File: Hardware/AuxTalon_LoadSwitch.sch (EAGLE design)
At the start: 89 parts, among them J1 CONN_AUX_M12_REMOTE, J2 CONN_AUX_M12_REMOTE, J3 CONN_AUX_M12_REMOTE, J4 CONN_TALON_REMOTE, U1 ADS1115, U11 MCP23018QFN, U16 MAX9064, U17 MAX9064, U18 SN74AUP1T87, U19 MAX9064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

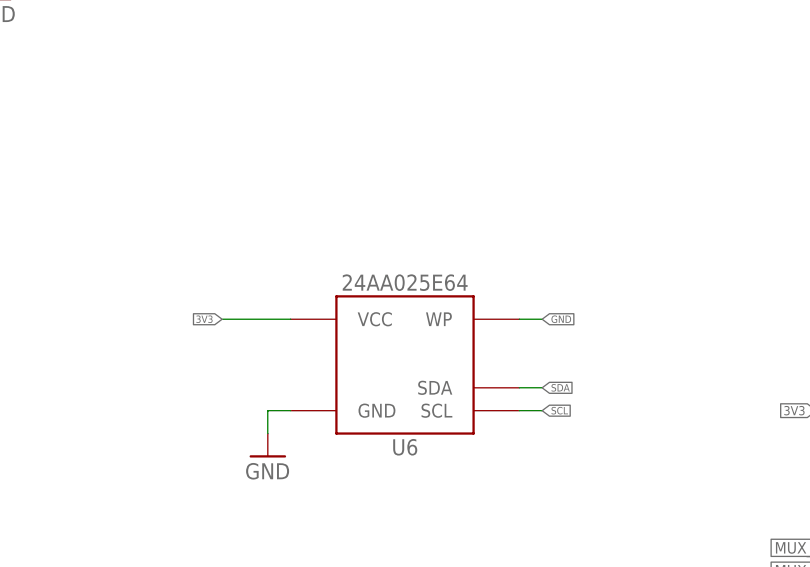
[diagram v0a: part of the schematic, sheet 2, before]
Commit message: Updates for modified BoM
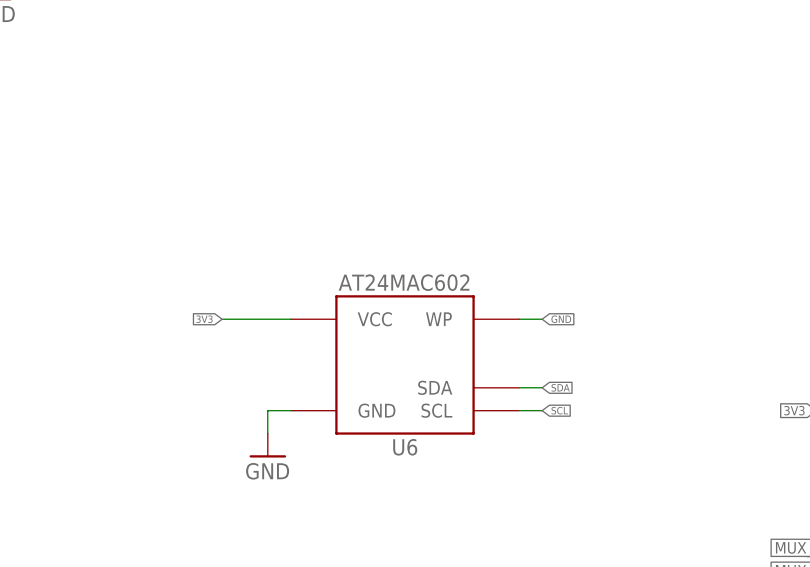
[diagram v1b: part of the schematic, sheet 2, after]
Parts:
- R10: device bschulz_passives:R-EU_100KR0402 -> bschulz_passives:R-EU_100KR0603
- U6: value 24AA02SOT23 -> AT24MAC602SOT23; device bschulz:24AA02SOT23 -> bschulz:AT24MAC602SOT23
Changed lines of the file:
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@@
 <part name="GND22" library="supply1" library_urn="urn:adsk.eagle:library:371" deviceset="GND" device=""/>
 <part name="GND23" library="supply1" library_urn="urn:adsk.eagle:library:371" deviceset="GND" device=""/>
-<part name="U6" library="bschulz" deviceset="24AA02" device="SOT23"/>
+<part name="U6" library="bschulz" deviceset="AT24MAC*02" device="SOT23" technology="6" value="AT24MAC602SOT23"/>
 <part name="GND24" library="supply1" library_urn="urn:adsk.eagle:library:371" deviceset="GND" device=""/>
 <part name="U7" library="bschulz" deviceset="74HC4852" device=""/>
@@
 <part name="C8" library="bschulz_passives" deviceset="C-EU" device="C0805" technology="10UF" value="10uF"/>
 <part name="GND51" library="supply1" library_urn="urn:adsk.eagle:library:371" deviceset="GND" device=""/>
-<part name="R10" library="bschulz_passives" deviceset="R-EU_" device="R0402" technology="100K" value="100k"/>
+<part name="R10" library="bschulz_passives" deviceset="R-EU_" device="R0603" technology="100K" value="100k"/>
 <part name="GND52" library="supply1" library_urn="urn:adsk.eagle:library:371" deviceset="GND" device=""/>
 <part name="GND53" library="supply1" library_urn="urn:adsk.eagle:library:371" deviceset="GND" device=""/>

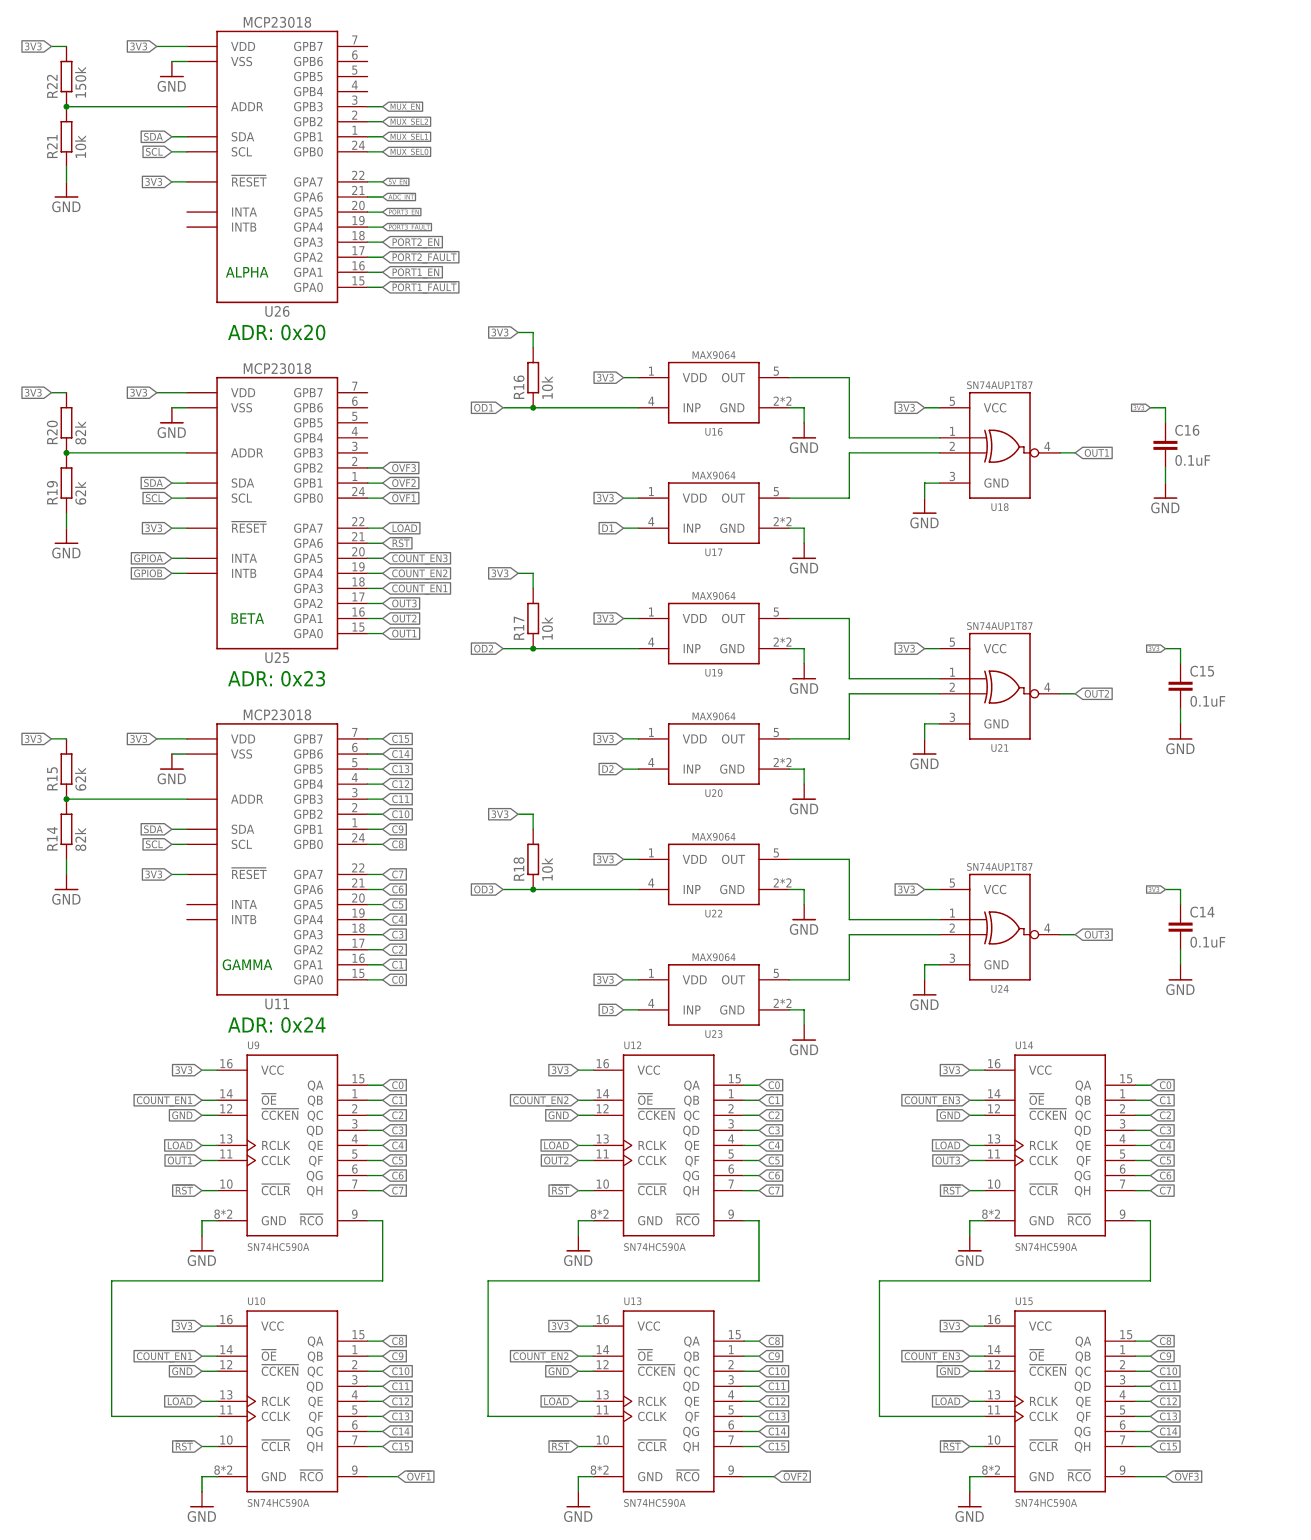
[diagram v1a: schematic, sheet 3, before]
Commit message: v1.4 Updates
Updated schematic and layout, boards sent to fab
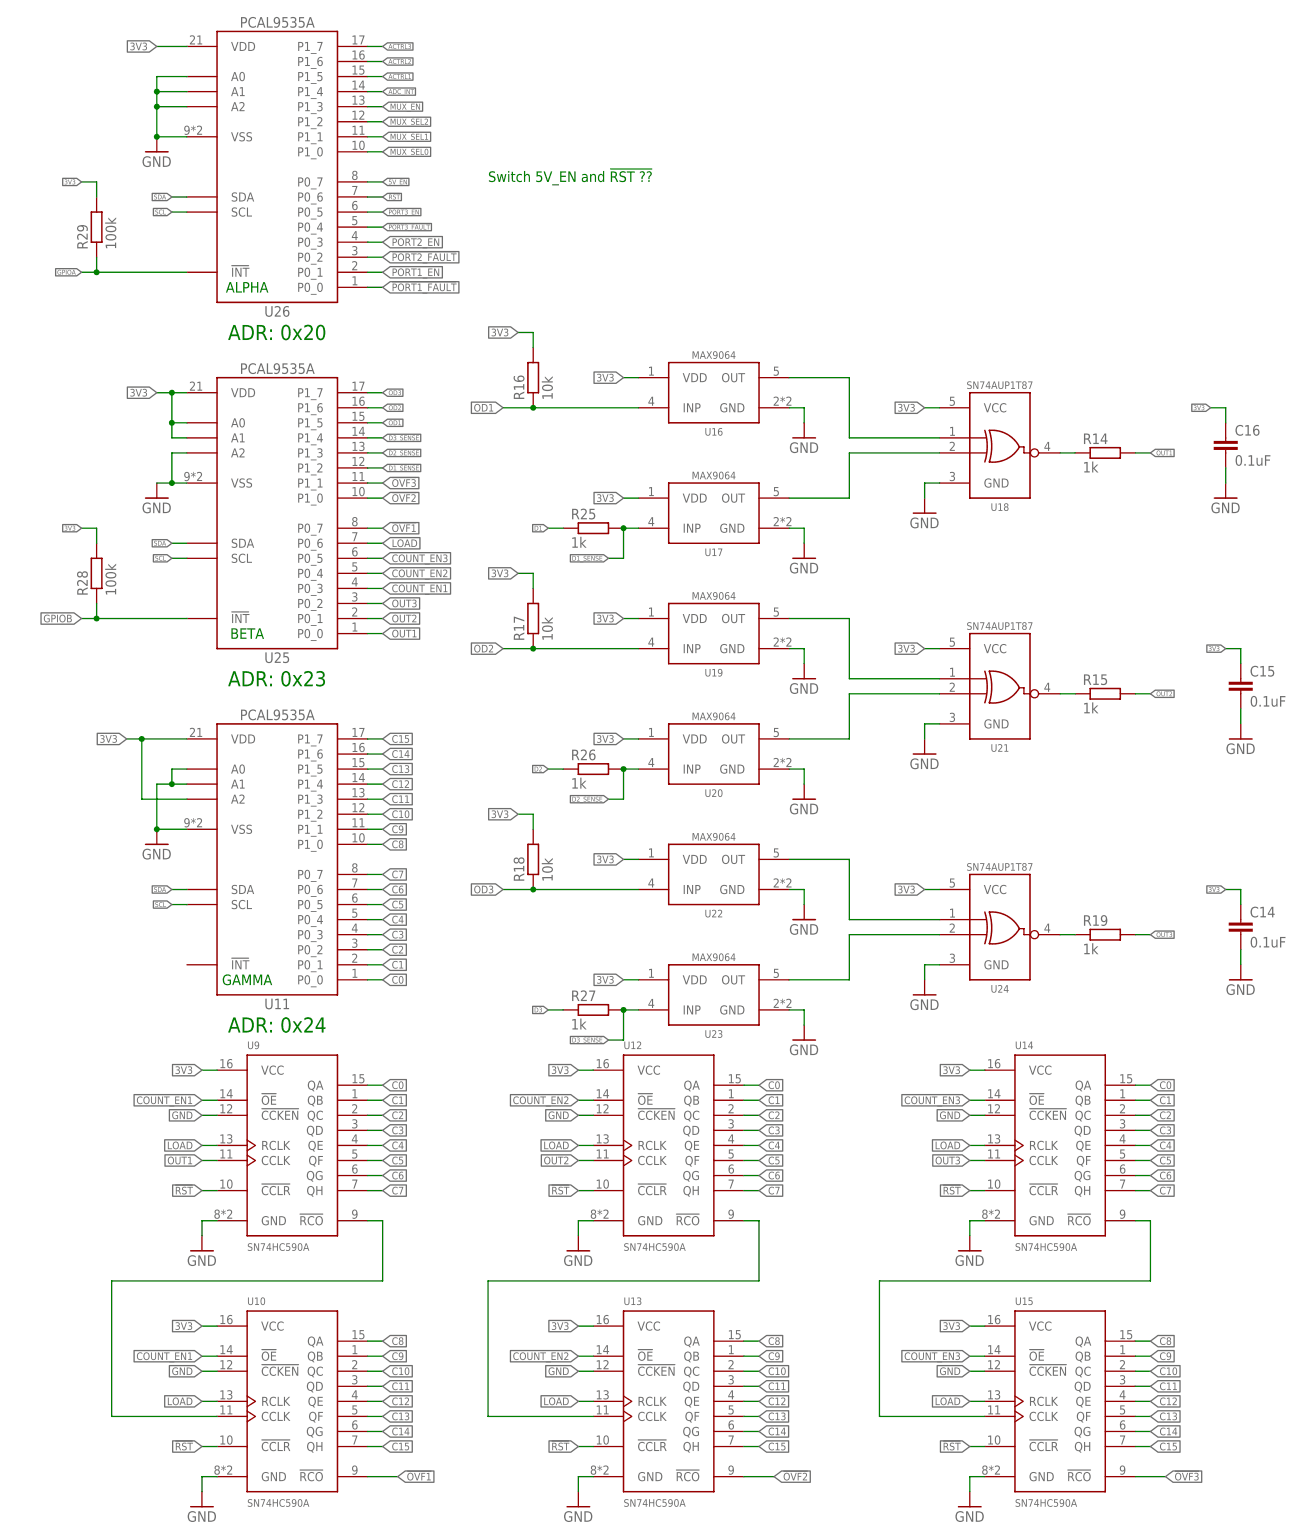
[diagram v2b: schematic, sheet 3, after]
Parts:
- added Q1, Q2, Q3: 2N7002, bschulz:MOSFET-NCH-2N7002P
- added R25, R26, R27: 1k, bschulz_passives:R-EU_1KR0402
- added R28, R29: 100k, bschulz_passives:R-EU_100KR0402
- R14: value 82k -> 1k; device bschulz_passives:R-EU_82KR0603 -> bschulz_passives:R-EU_1KR0402
- R15, R19: value 62k -> 1k; device bschulz_passives:R-EU_62KR0603 -> bschulz_passives:R-EU_1KR0402
- R20: value 82k -> 10k; device bschulz_passives:R-EU_82KR0603 -> bschulz_passives:R-EU_10KR0402
- R21: device bschulz_passives:R-EU_10KR0603 -> bschulz_passives:R-EU_10KR0402
- R22: value 150k -> 10k; device bschulz_passives:R-EU_150KR0603 -> bschulz_passives:R-EU_10KR0402
- U11, U25, U26: value MCP23018QFN -> PCAL9535AQFN; device bschulz:MCP23018QFN -> bschulz:PCAL9535AQFN
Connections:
- new net ACTRL1: Q1.G, U26.P1_5
- new net ACTRL2: Q2.G, U26.P1_6
- new net ACTRL3: Q3.G, U26.P1_7
- new net D1_SENSE: R25.2, U17.INP, U25.P1_2
- new net D2_SENSE: R26.2, U20.INP, U25.P1_3
- new net D3_SENSE: R27.2, U23.INP, U25.P1_4
- new net N$15: Q1.D, R20.1
- new net N$17: R15.1, U21.Y
- new net N$19: R19.1, U24.Y
- net !OVF1: now also U25.P0_7; no longer U25.GPB0
- net !OVF2: now also U25.P1_0; no longer U25.GPB1
- net !OVF3: now also U25.P1_1; no longer U25.GPB2
- net !PORT1_FAULT: now also U26.P0_0; no longer U26.GPA0
- net !PORT2_FAULT: now also U26.P0_2; no longer U26.GPA2
- net !PORT3_FAULT: now also U26.P0_4; no longer U26.GPA4
- net !RST: now also U26.P0_6; no longer U25.GPA6
- net 3V3: now also R28.2, R29.2, U11.A2, U25.A0, U25.A1; no longer R15.2, R20.2, R22.2, U11.!RESET, U25.!RESET, U26.!RESET
- net 5V_EN: now also U26.P0_7; no longer U26.GPA7
- net ADC_INT: now also U26.P1_4; no longer U26.GPA6
- net AIN1: now also R20.2
- net AIN2: now also R21.2
- net AIN3: now also R22.2
- net C0: now also U11.P0_0; no longer U11.GPA0
- net C1: now also U11.P0_1; no longer U11.GPA1
- net C10: now also U11.P1_2; no longer U11.GPB2
- net C11: now also U11.P1_3; no longer U11.GPB3
- net C12: now also U11.P1_4; no longer U11.GPB4
- net C13: now also U11.P1_5; no longer U11.GPB5
- net C14: now also U11.P1_6; no longer U11.GPB6
- net C15: now also U11.P1_7; no longer U11.GPB7
- net C2: now also U11.P0_2; no longer U11.GPA2
- net C3: now also U11.P0_3; no longer U11.GPA3
- net C4: now also U11.P0_4; no longer U11.GPA4
- net C5: now also U11.P0_5; no longer U11.GPA5
- net C6: now also U11.P0_6; no longer U11.GPA6
- net C7: now also U11.P0_7; no longer U11.GPA7
- net C8: now also U11.P1_0; no longer U11.GPB0
- net C9: now also U11.P1_1; no longer U11.GPB1
- net COUNT_EN1: now also U25.P0_3; no longer U25.GPA3
- net COUNT_EN2: now also U25.P0_4; no longer U25.GPA4
- net COUNT_EN3: now also U25.P0_5; no longer U25.GPA5
- net D1: now also R25.1; no longer U17.INP
- net D2: now also R26.1; no longer U20.INP
- net D3: now also R27.1; no longer U23.INP
- net GND: now also Q1.S, Q2.S, Q3.S, U11.A0, U11.A1, U25.A2, U26.A0, U26.A1, U26.A2; no longer R14.1, R19.1, R21.1
- net GPIOA: now also R29.1, U26.!INT; no longer U25.INTA
- net GPIOB: now also R28.1, U25.!INT; no longer U25.INTB
- net LOAD: now also U25.P0_6; no longer U25.GPA7
- net MUX_EN: now also U26.P1_3; no longer U26.GPB3
- net MUX_SEL0: now also U26.P1_0; no longer U26.GPB0
- net MUX_SEL1: now also U26.P1_1; no longer U26.GPB1
- net MUX_SEL2: now also U26.P1_2; no longer U26.GPB2
- net N$14: now also Q2.D, R21.1; no longer R21.2, R22.1, U26.ADDR
- net N$16: now also R14.1, U18.Y; no longer R19.2, R20.1, U25.ADDR
- net N$7: now also Q3.D, R22.1; no longer R14.2, R15.1, U11.ADDR
- net OD1: now also U25.P1_5
- net OD2: now also U25.P1_6
- net OD3: now also U25.P1_7
- net OUT1: now also R14.2, U25.P0_0; no longer U18.Y, U25.GPA0
- net OUT2: now also R15.2, U25.P0_1; no longer U21.Y, U25.GPA1
- net OUT3: now also R19.2, U25.P0_2; no longer U24.Y, U25.GPA2
- net PORT1_EN: now also U26.P0_1; no longer U26.GPA1
- net PORT2_EN: now also U26.P0_3; no longer U26.GPA3
- net PORT3_EN: now also U26.P0_5; no longer U26.GPA5
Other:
- note added: "Switch 5V_EN and !RST ??"
- moved on the sheet: C14, C15, C16, R14, R15, R19

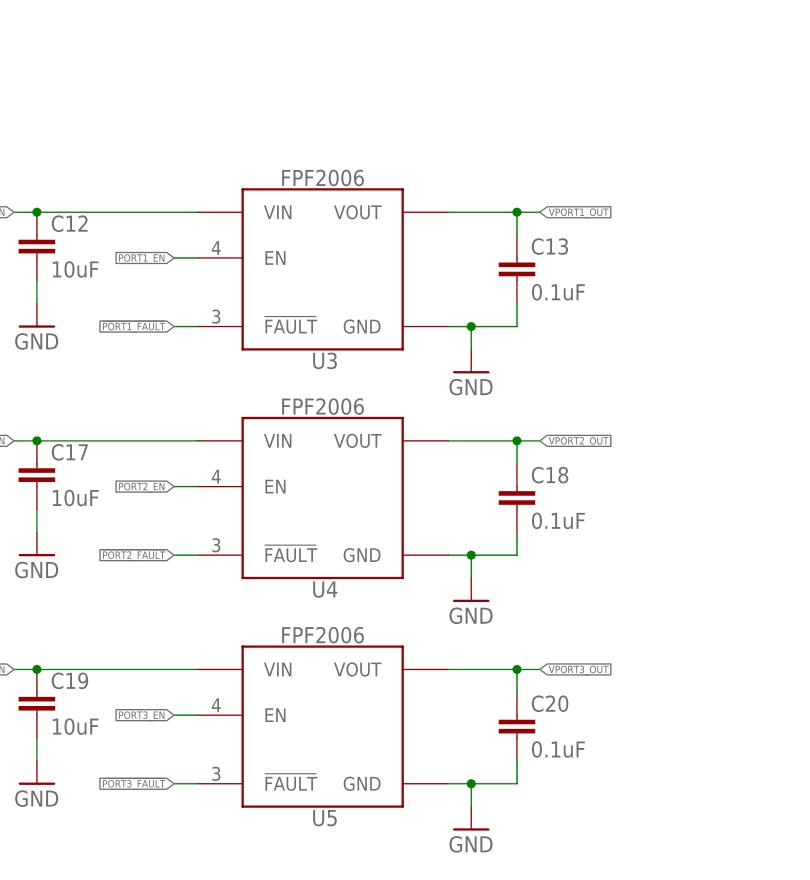
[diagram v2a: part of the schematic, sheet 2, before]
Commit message: Updates for v1.5
- Changed load switch
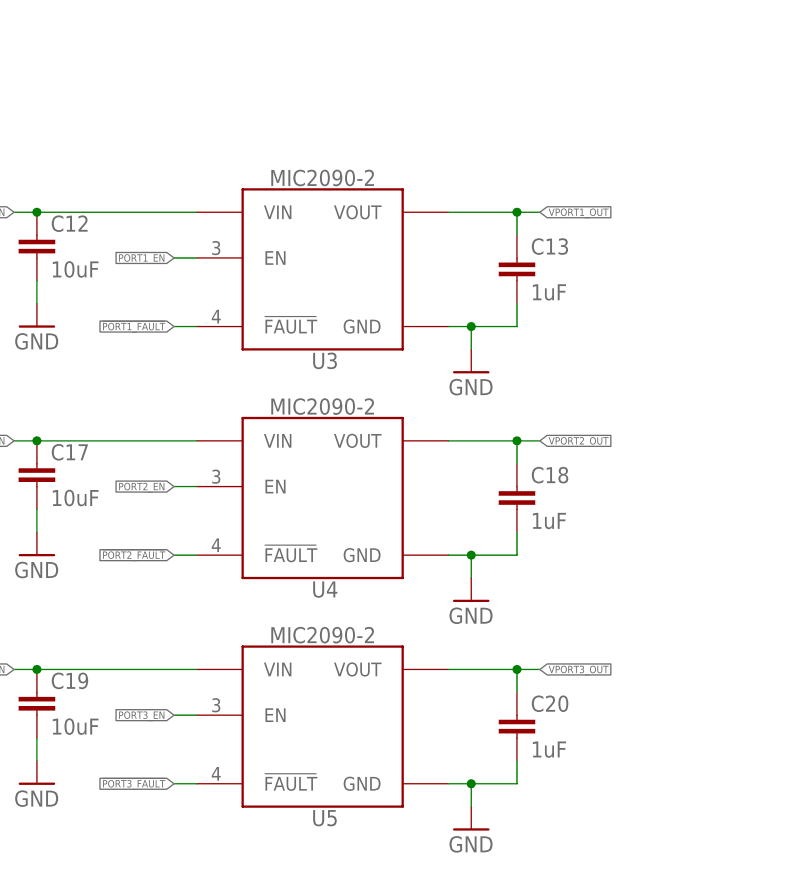
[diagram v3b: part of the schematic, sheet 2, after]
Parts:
- C13, C18, C20: value 0.1uF -> 1uF; device bschulz_passives:C-EU0.1UFC0402 -> bschulz_passives:C-EU1UFC0603
- U3, U4, U5: value TPS22944 -> MIC2090-2; device bschulz:TPS22944 -> bschulz:MIC2090-2; DIGIKEY 2156-FPF2006-ND -> (none); DISP FPF2006 -> (none); MF Fairchild -> (none); MPN FPF2006 -> (none)

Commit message: Changed Cout value
Changed `C13`, `C18`, `C20` from 1uF to 10uF
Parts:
- C13, C18, C20: value 1uF -> 10uF; device bschulz_passives:C-EU1UFC0603 -> bschulz_passives:C-EU10UFC0603
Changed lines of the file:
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@@
 <part name="GND12" library="supply1" library_urn="urn:adsk.eagle:library:371" deviceset="GND" device=""/>
 <part name="GND13" library="supply1" library_urn="urn:adsk.eagle:library:371" deviceset="GND" device=""/>
-<part name="C13" library="bschulz_passives" deviceset="C-EU" device="C0603" technology="1UF" value="1uF"/>
+<part name="C13" library="bschulz_passives" deviceset="C-EU" device="C0603" technology="10UF" value="10uF"/>
 <part name="C17" library="bschulz_passives" deviceset="C-EU" device="C0805" technology="10UF" value="10uF"/>
 <part name="GND14" library="supply1" library_urn="urn:adsk.eagle:library:371" deviceset="GND" device=""/>
 <part name="GND15" library="supply1" library_urn="urn:adsk.eagle:library:371" deviceset="GND" device=""/>
-<part name="C18" library="bschulz_passives" deviceset="C-EU" device="C0603" technology="1UF" value="1uF"/>
+<part name="C18" library="bschulz_passives" deviceset="C-EU" device="C0603" technology="10UF" value="10uF"/>
 <part name="C19" library="bschulz_passives" deviceset="C-EU" device="C0805" technology="10UF" value="10uF"/>
 <part name="GND16" library="supply1" library_urn="urn:adsk.eagle:library:371" deviceset="GND" device=""/>
 <part name="GND17" library="supply1" library_urn="urn:adsk.eagle:library:371" deviceset="GND" device=""/>
-<part name="C20" library="bschulz_passives" deviceset="C-EU" device="C0603" technology="1UF" value="1uF"/>
+<part name="C20" library="bschulz_passives" deviceset="C-EU" device="C0603" technology="10UF" value="10uF"/>
 <part name="D1" library="bschulz" deviceset="DIODE_ESD_BI" device="_0402" technology="_D5V0L1" value="6V"/>
 <part name="D2" library="bschulz" deviceset="DIODE_ESD_BI" device="_0402" technology="_D5V0L1" value="6V"/>
